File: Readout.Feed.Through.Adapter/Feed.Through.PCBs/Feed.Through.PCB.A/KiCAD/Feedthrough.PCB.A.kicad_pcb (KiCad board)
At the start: 2 copper layers, 80 x 80 mm, 20 parts

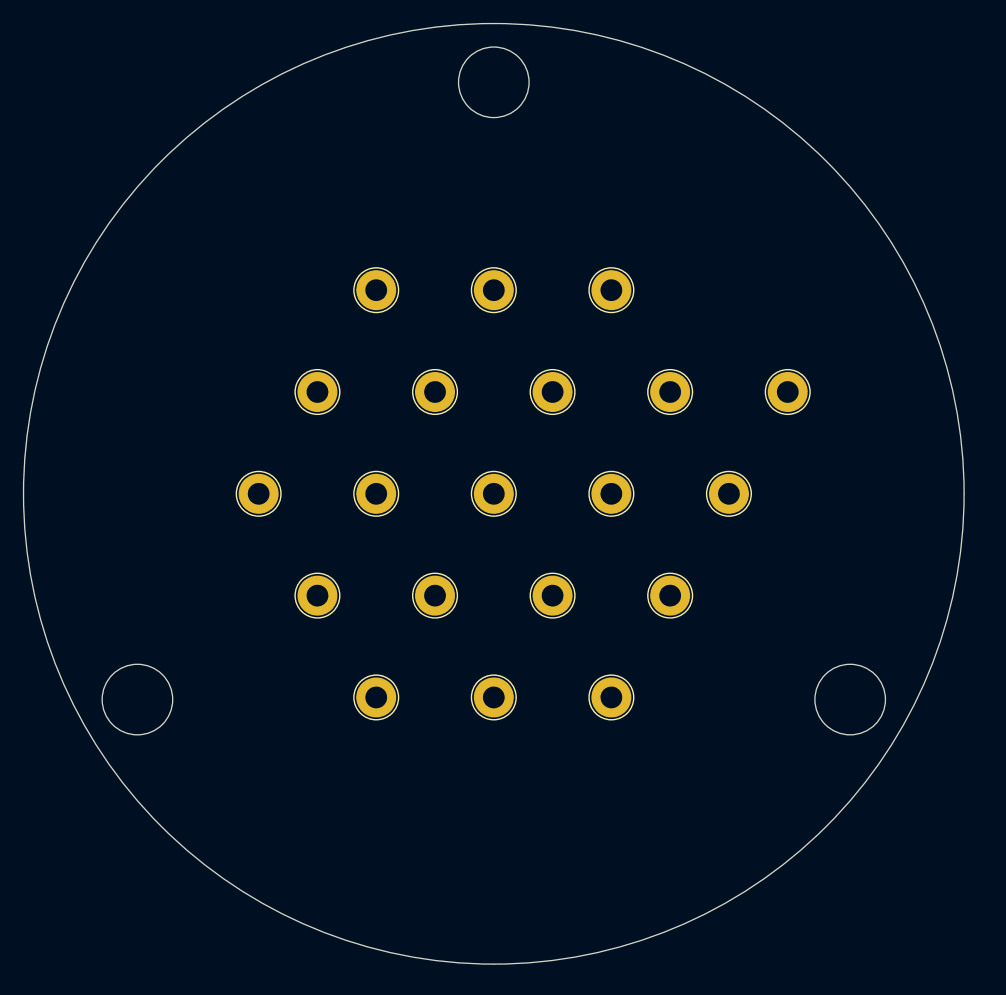
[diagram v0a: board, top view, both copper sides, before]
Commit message: Updated ReadoutPCBs to allow smoother gasflow
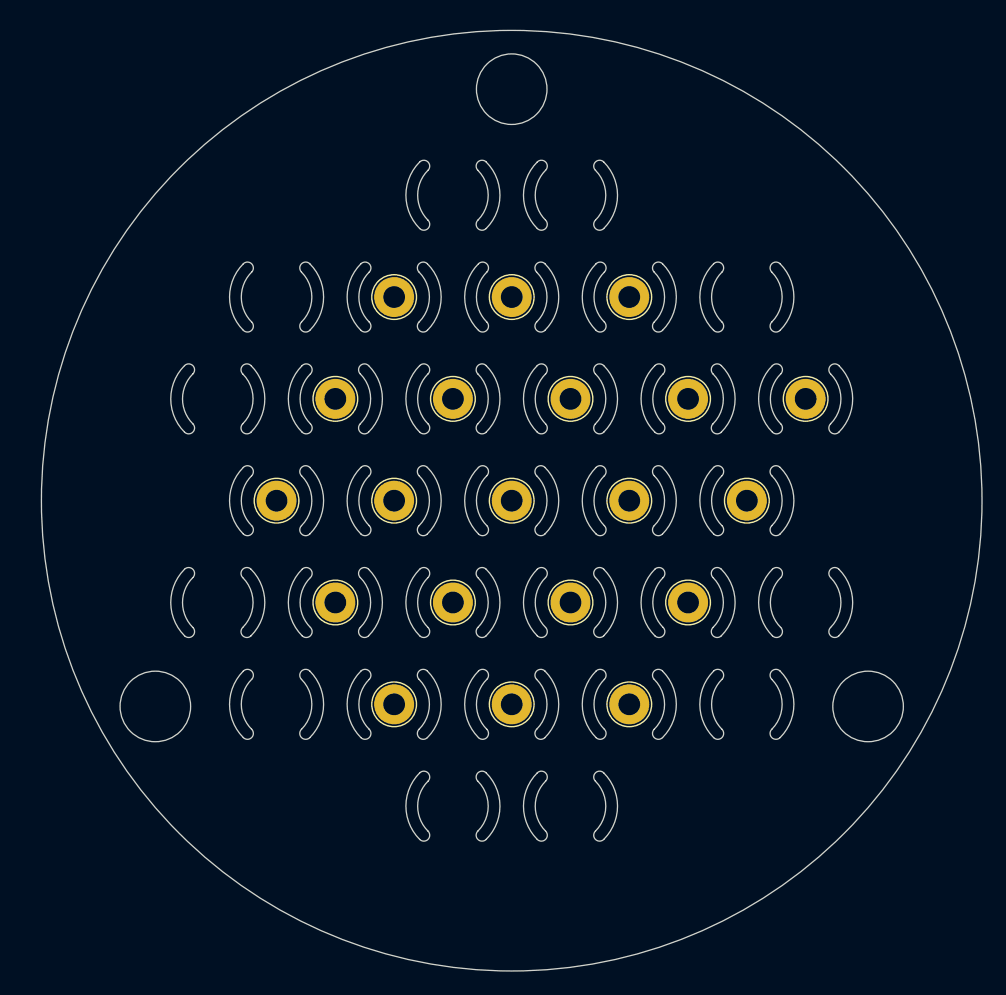
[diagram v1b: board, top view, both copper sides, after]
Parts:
- added G***: LOGO, LOGO, B.Cu at (64.7, 86.9)
- moved CH1 1.63 mm to (35.3, 53.9)
- moved CH1 1.63 mm to (40.3, 62.5)
- moved CH1 1.63 mm to (45.3, 36.6)
- moved CH10 1.63 mm to (65.3, 53.9)
- moved CH11 1.63 mm to (75.3, 53.9)
- moved CH12 1.63 mm to (50.3, 62.5)
- moved CH13 1.63 mm to (60.3, 62.5)
- moved CH14 1.63 mm to (70.3, 62.5)
- moved CH2 1.63 mm to (55.3, 36.6)
- moved CH3 1.63 mm to (65.3, 36.6)
- moved CH8 1.63 mm to (45.3, 53.9)
- moved CH9 1.63 mm to (55.3, 53.9)
- moved CH1 1.63 mm to (45.3, 71.2)
- moved CH1 1.63 mm to (40.3, 45.2)
- moved CH15 1.63 mm to (55.3, 71.2)
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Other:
- outline, holes or cut-outs redrawn
